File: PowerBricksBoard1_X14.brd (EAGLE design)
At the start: 160 x 100 mm, 16 parts

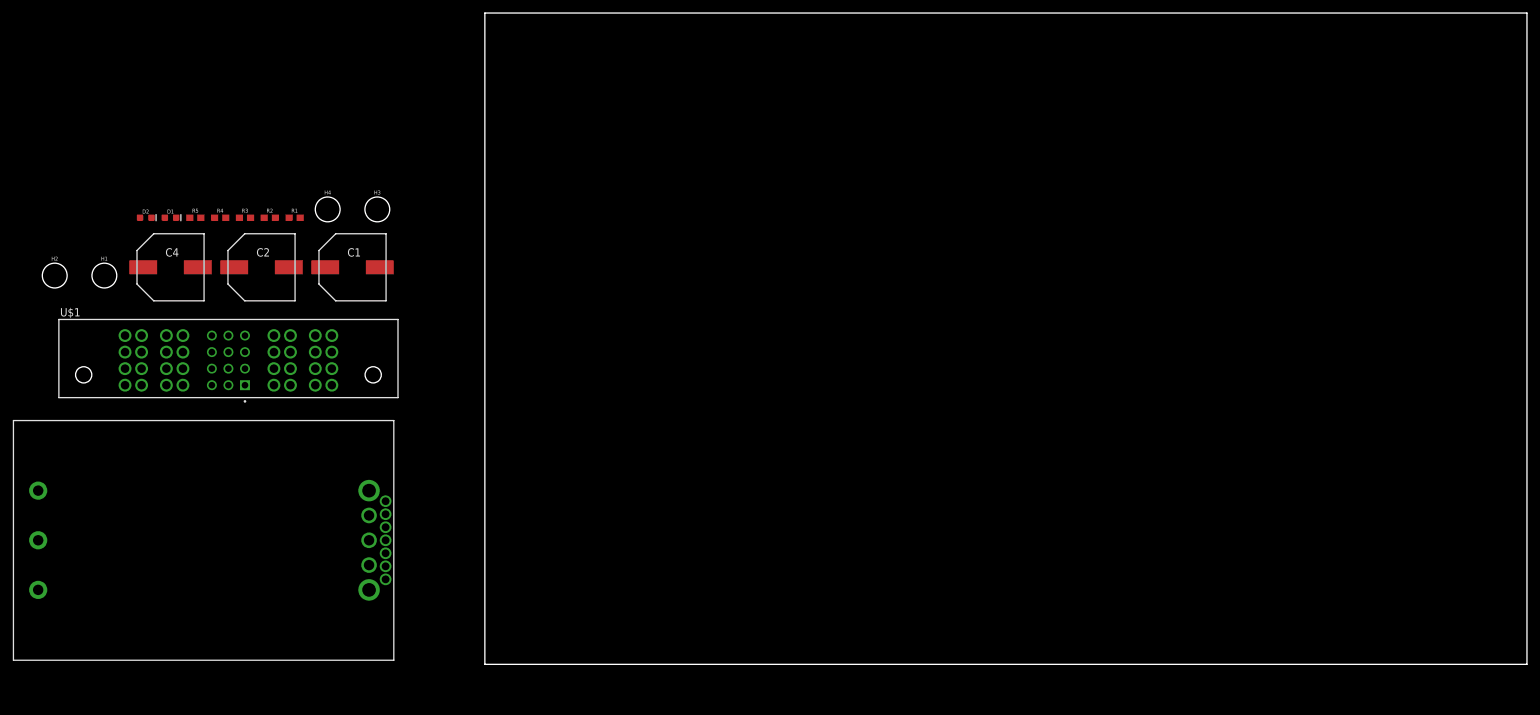
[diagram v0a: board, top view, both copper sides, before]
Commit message: adjusted board size
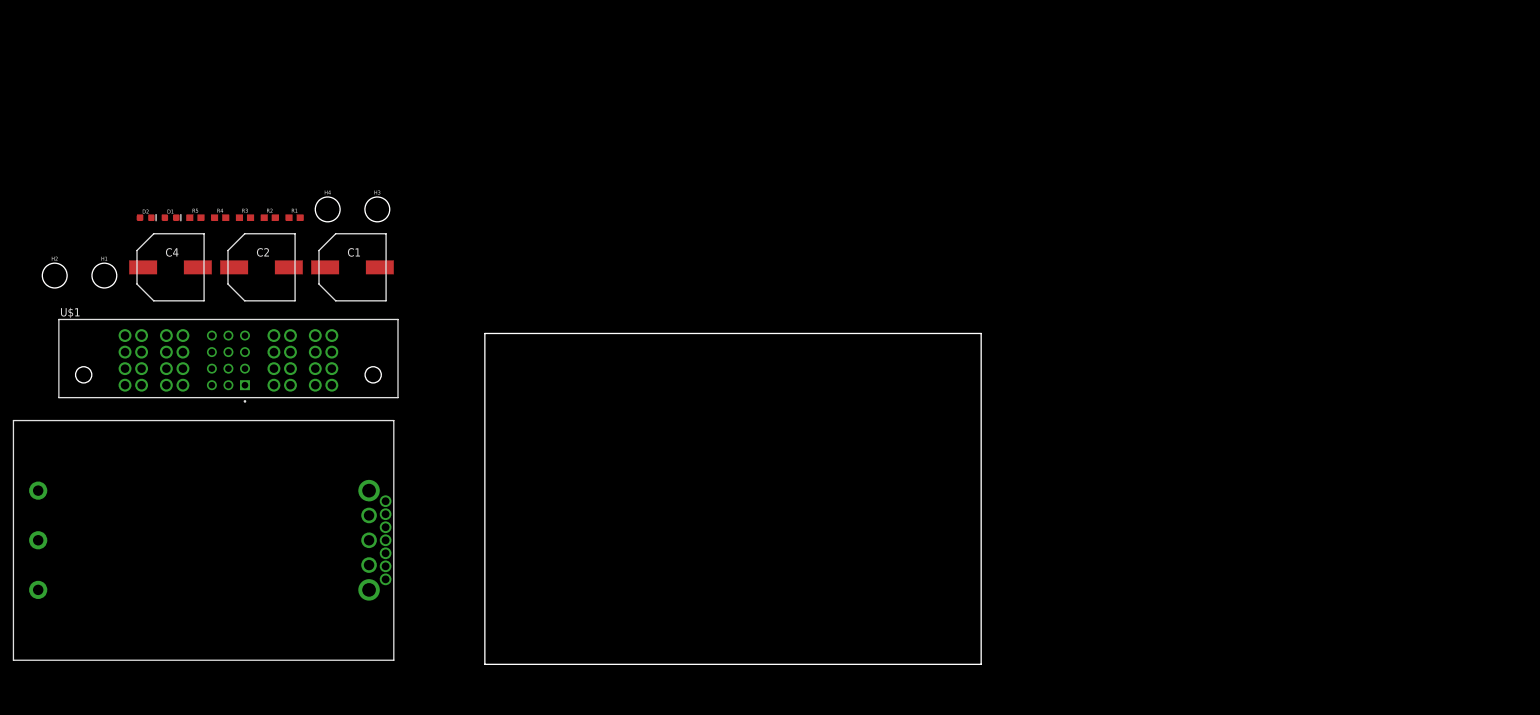
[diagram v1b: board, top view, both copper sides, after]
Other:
- board size 160 x 100 mm -> 76.2 x 50.8 mm
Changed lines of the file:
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@@
 <?xml version="1.0" encoding="utf-8"?>
 <!DOCTYPE eagle SYSTEM "eagle.dtd">
-<eagle version="9.6.2">
+<eagle version="9.5.0">
 <drawing>
 <settings>
@@
 <board>
 <plain>
-<wire x1="0" y1="0" x2="160" y2="0" width="0" layer="20"/>
-<wire x1="160" y1="0" x2="160" y2="100" width="0" layer="20"/>
-<wire x1="160" y1="100" x2="0" y2="100" width="0" layer="20"/>
-<wire x1="0" y1="100" x2="0" y2="0" width="0" layer="20"/>
+<wire x1="0" y1="0" x2="76.2" y2="0" width="0" layer="20"/>
+<wire x1="76.2" y1="0" x2="76.2" y2="50.8" width="0" layer="20"/>
+<wire x1="76.2" y1="50.8" x2="0" y2="50.8" width="0" layer="20"/>
+<wire x1="0" y1="50.8" x2="0" y2="0" width="0" layer="20"/>
 </plain>
 <attributes>

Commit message: Needed a design review and some bugs
DRC keepings giving me polygon priority issues
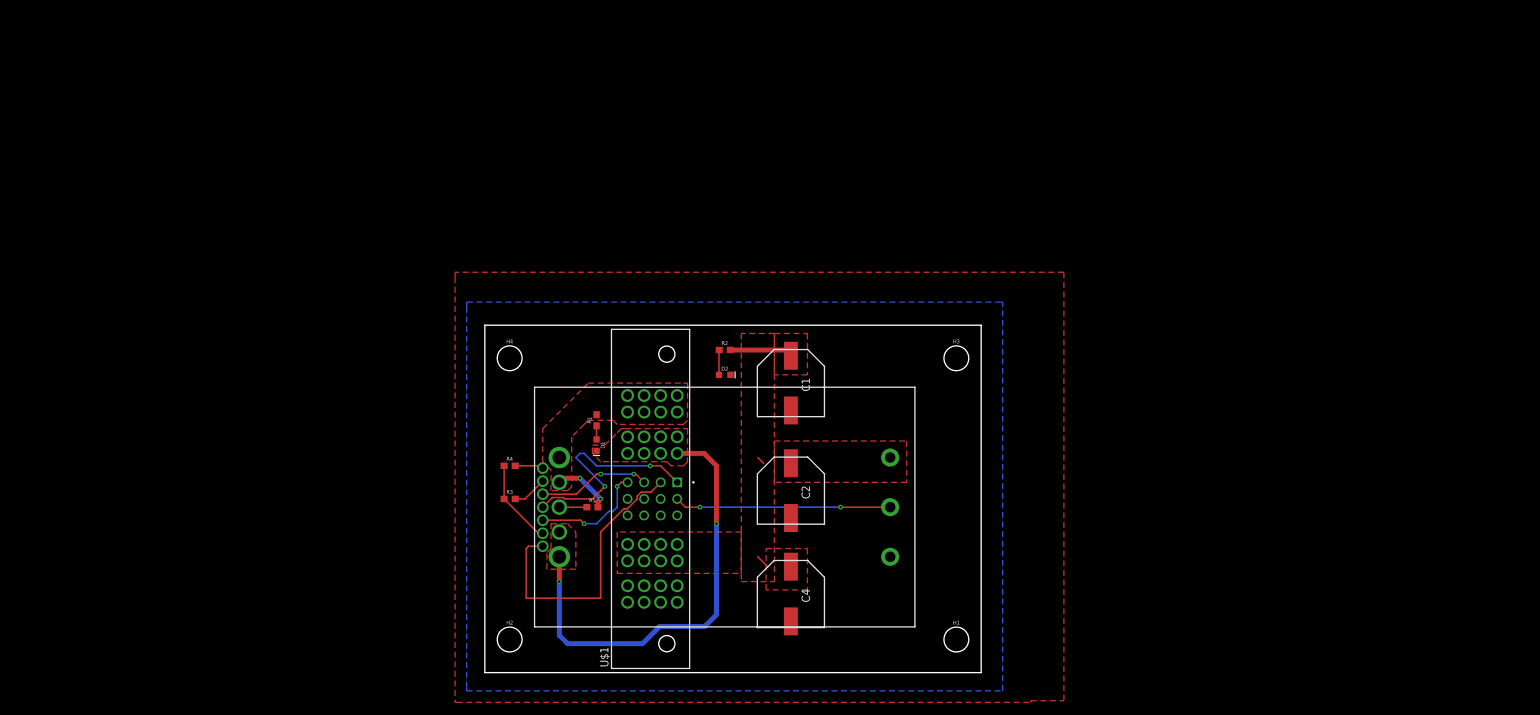
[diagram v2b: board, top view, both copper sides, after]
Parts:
- moved H1 142.2 mm to (72.4, 3.81)
- moved U$2 132.4 mm to (62.2, 31.8), turned to 180 degrees
- moved C4 107.7 mm to (47.0, 10.8), turned to 270 degrees
- moved D2 92.1 mm to (36.8, 44.5)
- moved H3 91.8 mm to (72.4, 47.0)
- moved H2 89.5 mm to (3.81, 3.81)
- moved C2 88.2 mm to (47.0, 26.7), turned to 270 degrees
- moved R5 75.4 mm to (16.5, 24.1)
- moved D1 74.1 mm to (17.1, 33.7), turned to 270 degrees
- moved R2 72.7 mm to (36.8, 48.3)
- moved U$1 70.0 mm to (27.9, 25.4), turned to 90 degrees
- moved C1 69.6 mm to (47.0, 43.2), turned to 270 degrees
- moved R3 59.3 mm to (3.81, 25.4)
- moved R4 58.5 mm to (3.81, 30.5)
- moved R1 55.8 mm to (17.1, 37.5), turned to 90 degrees
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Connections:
- removed net 12VGND: U$1.P02_1, U$1.P02_2, U$1.P02_3, U$1.P02_4, U$1.P02_5, U$1.P02_6, U$1.P02_7, U$1.P02_8
- net 12_GND: now also U$1.P02_1, U$1.P02_2, U$1.P02_3, U$1.P02_4, U$1.P02_5, U$1.P02_6, U$1.P02_7, U$1.P02_8
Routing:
- net 12_GND: track 0.00 -> 68.2 mm, vias 0 -> 2
- net C2: track 0.00 -> 44.5 mm
- net ALERT: track 0.00 -> 35.0 mm, vias 0 -> 2
- net ON/OFF: track 0.00 -> 33.2 mm, vias 0 -> 2
- net DATA: track 0.00 -> 17.7 mm, vias 0 -> 2
- net CLK: track 0.00 -> 17.4 mm, vias 0 -> 2
- net 48V: track 0.00 -> 13.2 mm
- net DGND: track 0.00 -> 13.2 mm
- net 12V: track 0.00 -> 9.37 mm, vias 0 -> 2
- net ADDR1: track 0.00 -> 5.36 mm
- net ADDR0: track 0.00 -> 4.37 mm
- net TRIM: track 0.00 -> 4.23 mm
- net N$2: track 0.00 -> 3.82 mm
- net N$1: track 0.00 -> 2.08 mm
- added copper zone on layer 1, net 12V
- added copper zone on layer 1, net 12_GND
- added copper zone on layer 1, net 48V
- added copper zone on layer 1, net 48_GND
- added copper zone on layer 16, net 48_GND
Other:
- board size 76.2 x 50.8 mm -> 76.2 x 53.3 mm

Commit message: update
erin plz help
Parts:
- moved D2 5.12 mm to (37.5, 49.5)
- moved R2 2.84 mm to (38.1, 45.7)
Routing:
- net 48_GND: track 0.00 -> 88.8 mm, vias 0 -> 1
- net 48V: track 13.2 -> 0.00 mm
- net 12_GND: track 68.2 -> 73.2 mm
- net 12V: track 9.37 -> 8.85 mm
- added copper zone on layer 16, net 12_GND
